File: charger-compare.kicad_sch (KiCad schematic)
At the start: 20 parts, among them J1 2.5x5.5mm, J3 Batt, J4 2.5x5.5mm, J5 TYPE-C16PIN, Q1 HL2304, U2 CH224Q

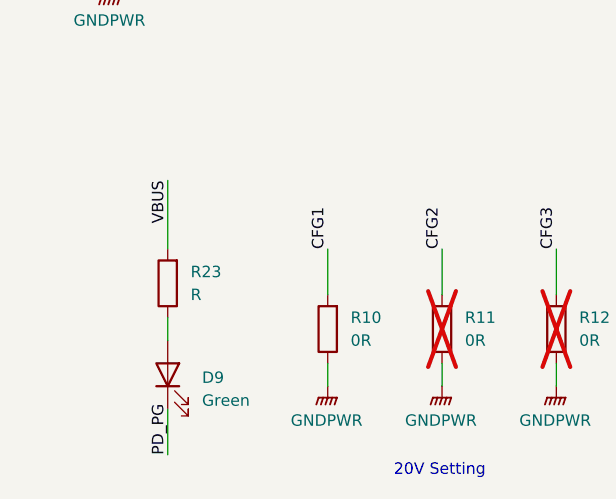
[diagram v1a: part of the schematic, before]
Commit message: Set LED resistors
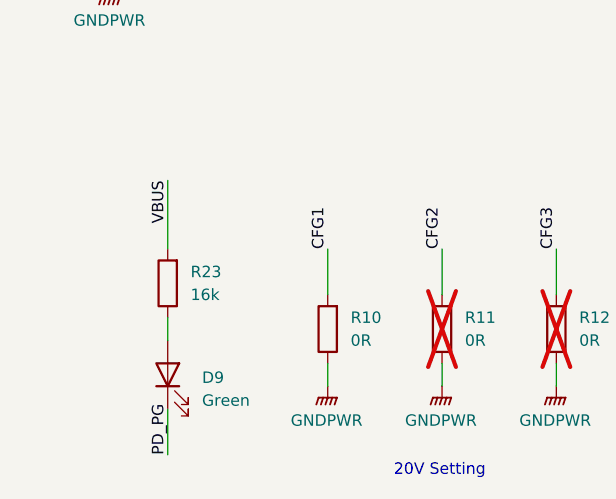
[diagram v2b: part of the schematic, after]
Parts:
- R23: value R -> 16k
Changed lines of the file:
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@@
 		(fields_autoplaced yes)
 		(property "Reference" "R23"
-			(at 48.26 166.37 0)
+			(at 48.26 166.3699 0)
 			(effects
 				(font
@@
 			)
 		)
-		(property "Value" "R"
-			(at 48.26 168.91 0)
+		(property "Value" "16k"
+			(at 48.26 168.9099 0)
 			(effects
 				(font

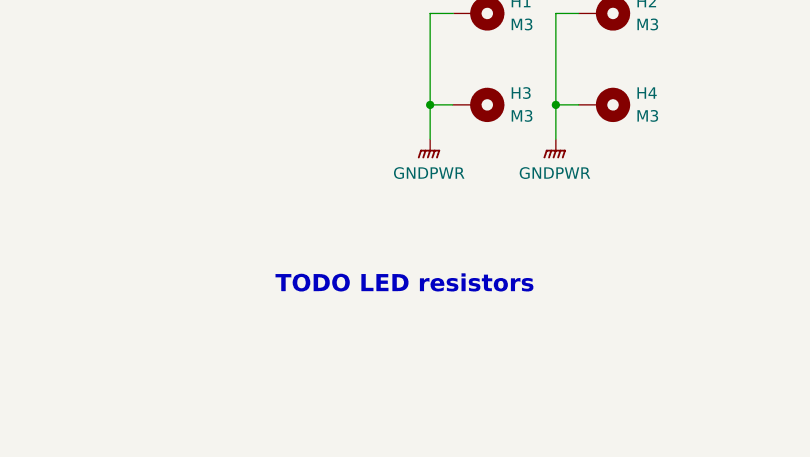
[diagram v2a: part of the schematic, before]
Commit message: Switch to JST-PH connectors Add Sheet titles
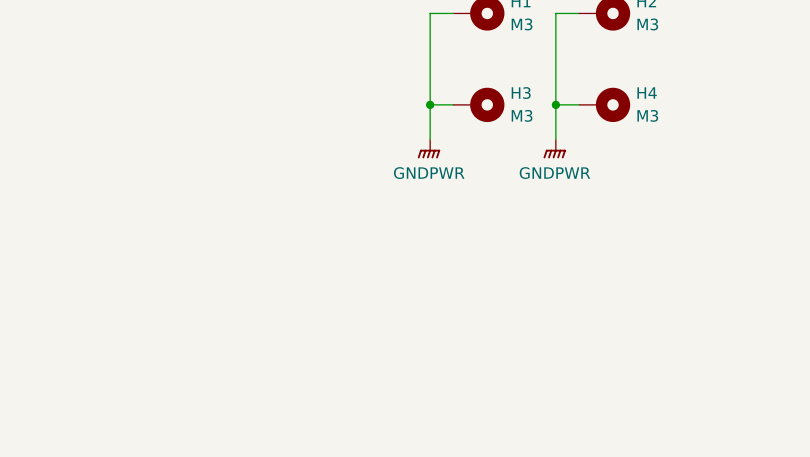
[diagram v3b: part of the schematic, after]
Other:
- note removed: "TODO LED resistors"
- title: BQ25792 Test Board -> 3S LiPo Charger Test Board
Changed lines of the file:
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@@
 	(paper "A4")
 	(title_block
-		(title "BQ25792 Test Board")
+		(title "3S LiPo Charger Test Board")
 		(rev "1.0")
+		(comment 1 "Through-hole connectors not to be installed as part of PCBA")
 	)
 	(text "20V USB-PD trigger"
@@
 				(bold yes)
 			)
-		)
-	)
-	(text "TODO LED resistors"
-		(exclude_from_sim no)
-		(at 209.296 172.466 0)
-		(effects
-			(font
-				(size 1.905 1.905)
-				(thickness 0.381)
-				(bold yes)
-			)

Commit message: Action review feedback
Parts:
- added R37: 0R, Resistor_SMD:R_1206_3216Metric, symbol Device:R
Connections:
- net VBUS: now also R37.1; no longer J4.1
- new net MP2759 Buck/VIN: J4.1, R37.2
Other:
- note added: "20V Setting CFG2&3 have an internal pull-up"
- note removed: "20V Setting"
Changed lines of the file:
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@@
 		)
 	)
-	(text "20V Setting"
+	(text "20V Setting\nCFG2&3 have an internal pull-up"
 		(exclude_from_sim no)
 		(at 75.946 188.468 0)
@@
 	(text "Reduced current below 18V"
 		(exclude_from_sim no)
-		(at 145.796 88.9 0)
+		(at 151.638 88.9 0)
 		(effects
 			(font
@@
 	(text "15-32V 3A Buck Charger"
 		(exclude_from_sim no)
-		(at 145.542 85.852 0)
+		(at 151.384 85.852 0)
 		(effects
 			(font
@@
 	)
 	(junction
-		(at 118.11 101.6)
-		(diameter 0)
-		(color 0 0 0 0)
-	)
-	(junction
 		(at 226.06 152.4)
 		(diameter 0)
@@
 	)
 	(junction
+		(at 118.11 101.6)
+		(diameter 0)
+		(color 0 0 0 0)
+	)
+	(junction
 		(at 92.71 104.14)
 		(diameter 0)
@@
 	(wire
 		(pts
-			(xy 118.11 101.6) (xy 118.11 88.9)
+			(xy 39.37 132.08) (xy 39.37 134.62)
 		)
 		(stroke
@@
 	(wire
 		(pts
-			(xy 39.37 132.08) (xy 39.37 134.62)
+			(xy 110.49 130.81) (xy 113.03 130.81)
 		)
 		(stroke
@@
 	(wire
 		(pts
-			(xy 110.49 130.81) (xy 113.03 130.81)
+			(xy 57.15 109.22) (xy 57.15 111.76)
 		)
 		(stroke
@@
 	(wire
 		(pts
-			(xy 57.15 109.22) (xy 57.15 111.76)
+			(xy 184.15 101.6) (xy 184.15 82.55)
 		)
 		(stroke
@@
 	(wire
 		(pts
-			(xy 184.15 101.6) (xy 184.15 82.55)
+			(xy 246.38 95.25) (xy 246.38 101.6)
 		)
 		(stroke
@@
 	(wire
 		(pts
-			(xy 246.38 95.25) (xy 246.38 101.6)
+			(xy 118.11 99.06) (xy 118.11 101.6)
 		)
 		(stroke
@@
 	(wire
 		(pts
-			(xy 118.11 101.6) (xy 124.46 101.6)
+			(xy 118.11 101.6) (xy 129.54 101.6)
 		)
 		(stroke
@@
 	(wire
 		(pts
+			(xy 118.11 88.9) (xy 118.11 91.44)
+		)
+		(stroke
+			(width 0)
+			(type default)
+		)
+	)
+	(wire
+		(pts
 			(xy 54.61 104.14) (xy 57.15 104.14)
 		)
@@
 	(wire
 		(pts
-			(xy 184.15 101.6) (xy 167.64 101.6)
+			(xy 184.15 101.6) (xy 172.72 101.6)
 		)
 		(stroke
@@
 	)
 	(symbol
+		(lib_id "Device:R")
+		(at 118.11 95.25 0)
+		(unit 1)
+		(exclude_from_sim no)
+		(in_bom yes)
+		(on_board yes)
+		(dnp no)
+		(fields_autoplaced yes)
+		(property "Reference" "R37"
+			(at 120.65 93.9799 0)
+			(effects
+				(font
+					(size 1.27 1.27)
+				)
+				(justify left)
+			)
+		)
+		(property "Value" "0R"
+			(at 120.65 96.5199 0)
+			(effects
+				(font
+					(size 1.27 1.27)
+				)
+				(justify left)
+			)
+		)
+		(property "Footprint" "Resistor_SMD:R_1206_3216Metric"
+			(at 116.332 95.25 90)
+			(effects
+				(font
+					(size 1.27 1.27)
+				)
+				(hide yes)
+			)
+		)
+		(property "Datasheet" "~"
+			(at 118.11 95.25 0)
+			(effects
+				(font
+					(size 1.27 1.27)
+				)
+				(hide yes)
+			)
+		)
+		(property "Description" "Resistor"
+			(at 118.11 95.25 0)
+			(effects
+				(font
+					(size 1.27 1.27)
+				)
+				(hide yes)
+			)
+		)
+		(pin "1"
+		)
+		(pin "2"
+		)
+		(instances
+			(project ""
+				(path "/1ee3bb19-9ed0-41e9-a9ff-1e5d7db780de"
+					(reference "R37")
+					(unit 1)
+				)
+			)
+		)
+	)
+	(symbol
 		(lib_id "power:GNDPWR")
 		(at 226.06 156.21 0)
@@
 	)
 	(sheet
-		(at 124.46 93.98)
+		(at 129.54 93.98)
 		(size 43.18 26.67)
 		(exclude_from_sim no)
@@
 		)
 		(property "Sheetname" "MP2759 Buck"
-			(at 124.46 93.2684 0)
+			(at 129.54 93.2684 0)
 			(effects
 				(font
@@
 		)
 		(property "Sheetfile" "MP2759.kicad_sch"
-			(at 124.46 121.2346 0)
+			(at 129.54 121.2346 0)
 			(effects
 				(font
@@
 		)
 		(pin "VIN" input
-			(at 124.46 101.6 180)
+			(at 129.54 101.6 180)
 			(effects
 				(font
@@
 		)
 		(pin "BATT+" output
-			(at 167.64 101.6 0)
+			(at 172.72 101.6 0)
 			(effects
 				(font
